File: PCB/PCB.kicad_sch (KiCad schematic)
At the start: 10 parts, among them SW1 Bourns PEC11R, SW2 Bourns PEC11R, SW3 SW_DPST, SW4 SW_DPST, SW5 SW_DPST, U1 RPi_Pico_TH, U2 RDA5807M_Module, U3 LM386

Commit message: finished rev 0 of circuit schematic
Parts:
- added C1: 0.047u, symbol Device:C
- added C2, C3: 470uF, symbol Device:C
- added C4, C5, C6, C7: 0.01uF, Capacitor_THT:C_Disc_D6.0mm_W2.5mm_P5.00mm, symbol Device:C
- added R1, R2: 2k, Resistor_THT:R_Axial_DIN0207_L6.3mm_D2.5mm_P7.62mm_Horizontal, symbol Device:R
- added R10, R11, R4, R5, R6, R7, R8, R9: 10k, Resistor_THT:R_Axial_DIN0207_L6.3mm_D2.5mm_P7.62mm_Horizontal, symbol Device:R
- added R3: 10, Resistor_THT:R_Axial_DIN0207_L6.3mm_D2.5mm_P7.62mm_Horizontal, symbol Device:R
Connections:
- net 3V3: now also SW3.1, SW4.1, SW5.1, C3.2, R1.1, R11.1, R2.1, R4.1, R6.1, R8.1
- net GND: now also DISP1.1 (VSS/GND), LS1.2, U2.6 (GND), U3.2 (-), U3.4 (GND), C3.1, C4.2, C5.2, C6.2, C7.2, R3.2
- net Radio sdio: now reaches U2.1 (SDIO)
- net Radio sdio: now also U1.32 (GP27/ADC1), R1.2
- net antenna: now reaches U2.10 (FMIN)
- net Radio sclk: now reaches U2.2 (SCLK)
- net Radio sclk: now also U1.31 (GP26/ADC0), R2.2
- net at U2.8 (LOUT): now also U3.3 (+)
- net Display sck: now reaches DISP1.3 (SCLK)
- net Display sck: now also U1.24 (GP18)
- net Display sda: now reaches DISP1.4 (SDA)
- net Display sda: now also U1.25 (GP19)
- net Display res: now reaches DISP1.5 (RES)
- net Display res: now also U1.27 (GP21)
- net Display DC: now reaches DISP1.6 (DC)
- net Display DC: now also U1.26 (GP20)
- net Display CS: now reaches DISP1.7 (CS)
- net Display CS: now also U1.22 (GP17)
- net at SW1.A: now also R4.2, R5.1
- net at SW1.B: now also R6.2, R7.1
- net Encoder1SW: now reaches SW1.S2
- net Encoder1SW: now also U1.4 (GP2)
- net B2: now reaches SW4.4
- net B2: now also U1.10 (GP7)
- net Encoder1A: now reaches U1.1 (GP0)
- net Encoder1A: now also C4.1, R5.2
- net B3: now reaches U1.11 (GP8)
- net B3: now also SW5.4
- net Encoder1B: now reaches U1.2 (GP1)
- net Encoder1B: now also C5.1, R7.2
- net Encoder2A: now reaches U1.5 (GP3)
- net Encoder2A: now also C6.1, R9.2
- net Encoder2B: now reaches U1.6 (GP4)
- net Encoder2B: now also C7.1, R10.2
- net Encoder2SW: now reaches U1.7 (GP5)
- net Encoder2SW: now also SW2.S2
- net B1: now reaches U1.9 (GP6)
- net B1: now also SW3.4
- net at SW2.A: now also R8.2, R9.1
- net at SW2.B: now also R10.1, R11.2
- net at LS1.1: now also C2.2
- net at U3.5: now also C1.1, C2.1
- new net: C1.2, R3.1
- no-connect marks 11 -> 30
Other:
- note added: "0"
- note added: "2025/06/20"
- note added: "Watering hole clock radio"
- note added: "Wil Fehr"
- moved on the sheet: DISP1, LS1, SW1, U2, U3

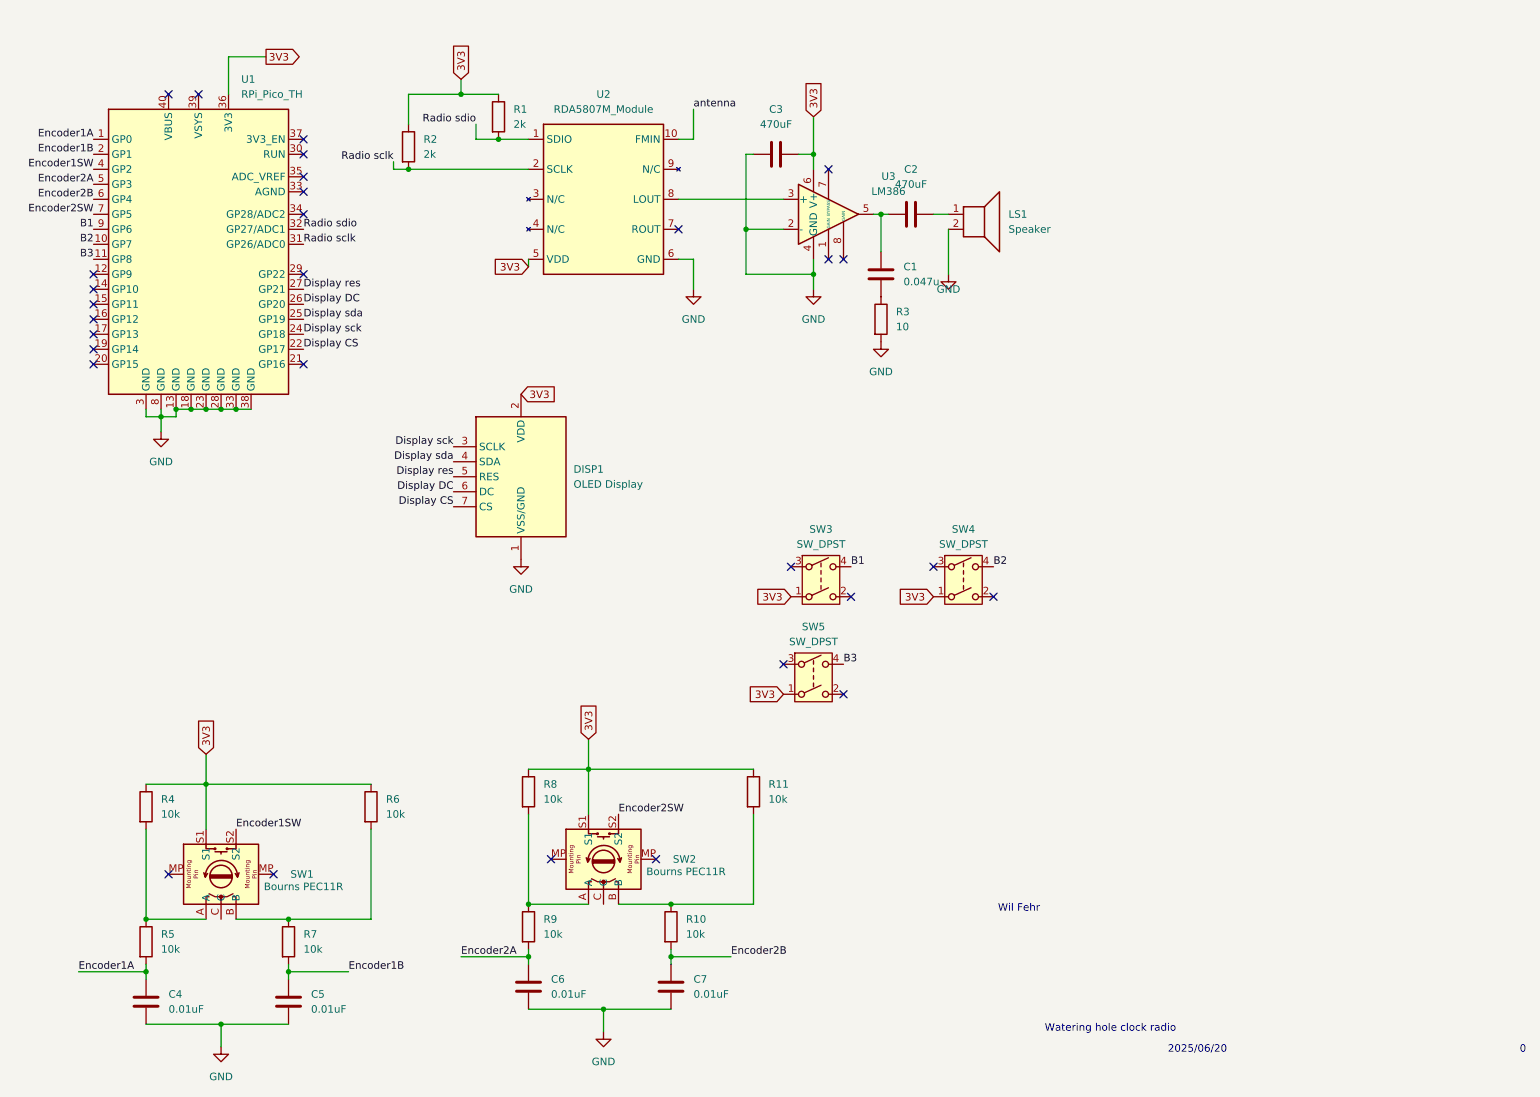
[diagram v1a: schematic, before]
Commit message: Initial look-over
Added footprint for LM386. We will need to decide footprints for resistors, capacitors, etc.

Any two legged through hole components can probably use the same footprint, but some components might be surface mount.
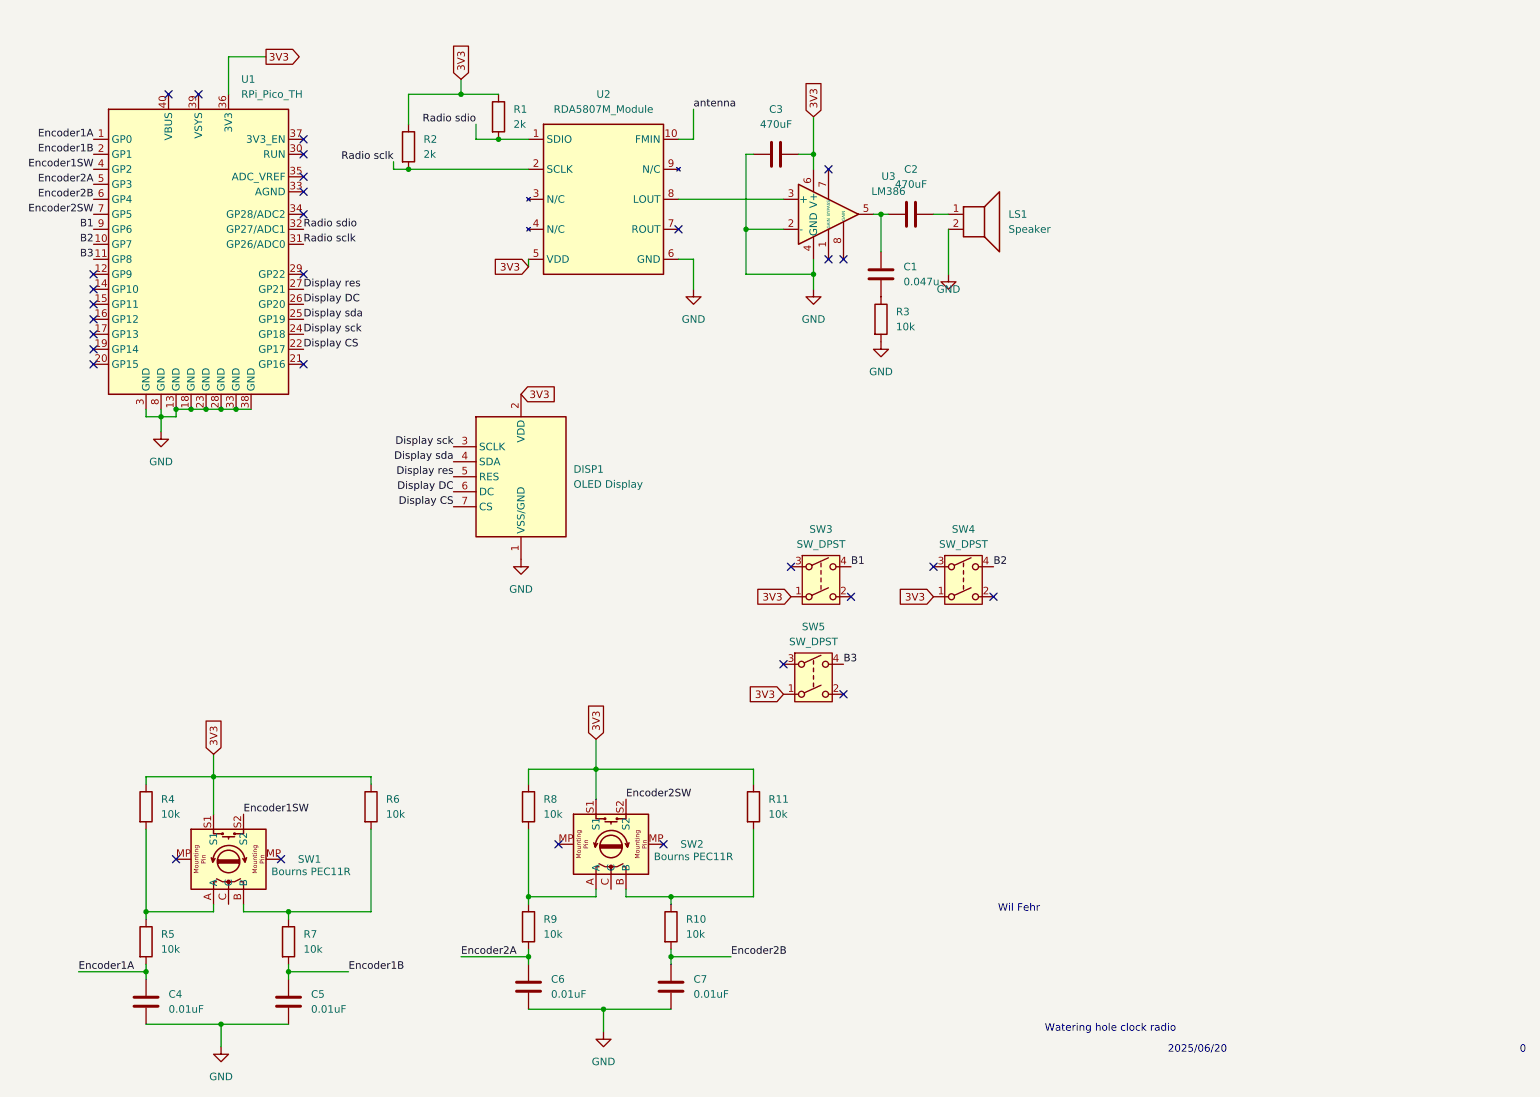
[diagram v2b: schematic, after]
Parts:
- R3: value 10 -> 10k
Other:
- moved on the sheet: R11, R8, SW1, SW2

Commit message: Added footprint to OLED
added 7pin screw terminal footprint to oled. Could not find OLED footprint so with this design we will just wire from OLED to screw terminal block.
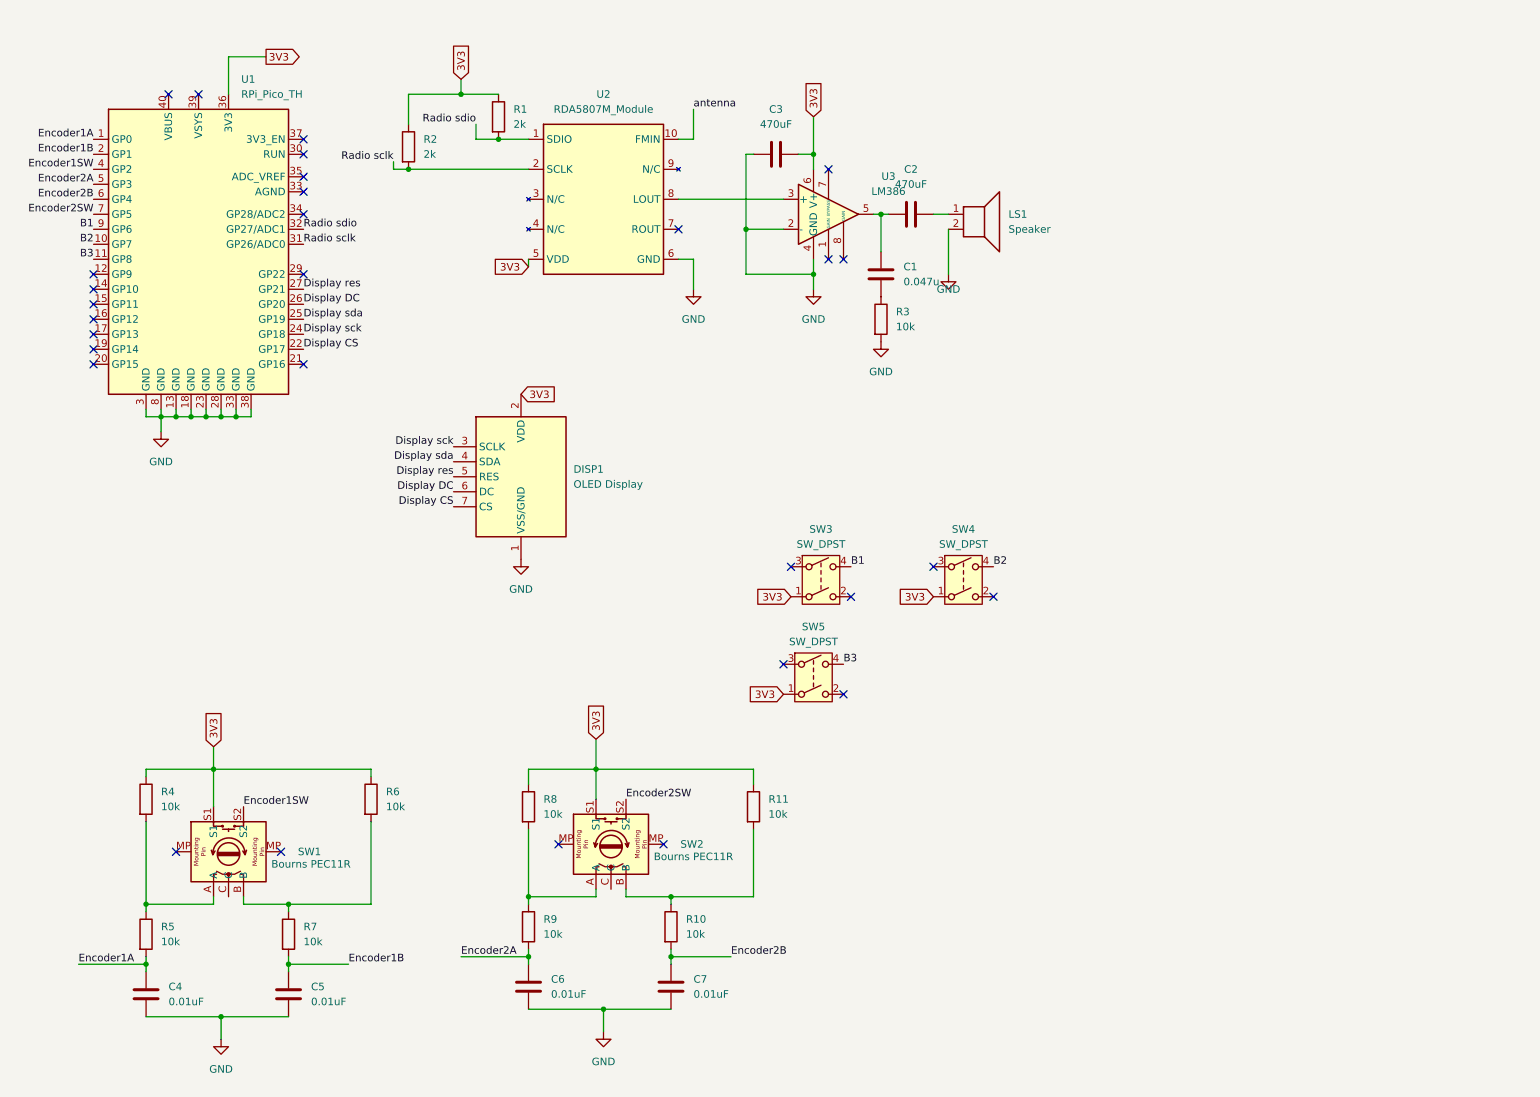
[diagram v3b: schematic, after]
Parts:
- C1, U3: footprint (none) -> LM386N_4_NOPB:DIP794W45P254L959H508Q8
- DISP1: footprint (none) -> 7pin_ScrewTerminal:1727065
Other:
- note removed: "0"
- note removed: "2025/06/20"
- note removed: "Watering hole clock radio"
- note removed: "Wil Fehr"
- company: (none) -> Wil Fehr & Aodhan Tonnesen
- title: (none) -> Watering Hole Clock Radio
- moved on the sheet: C4, C5, R4, R5, R6, R7, SW1

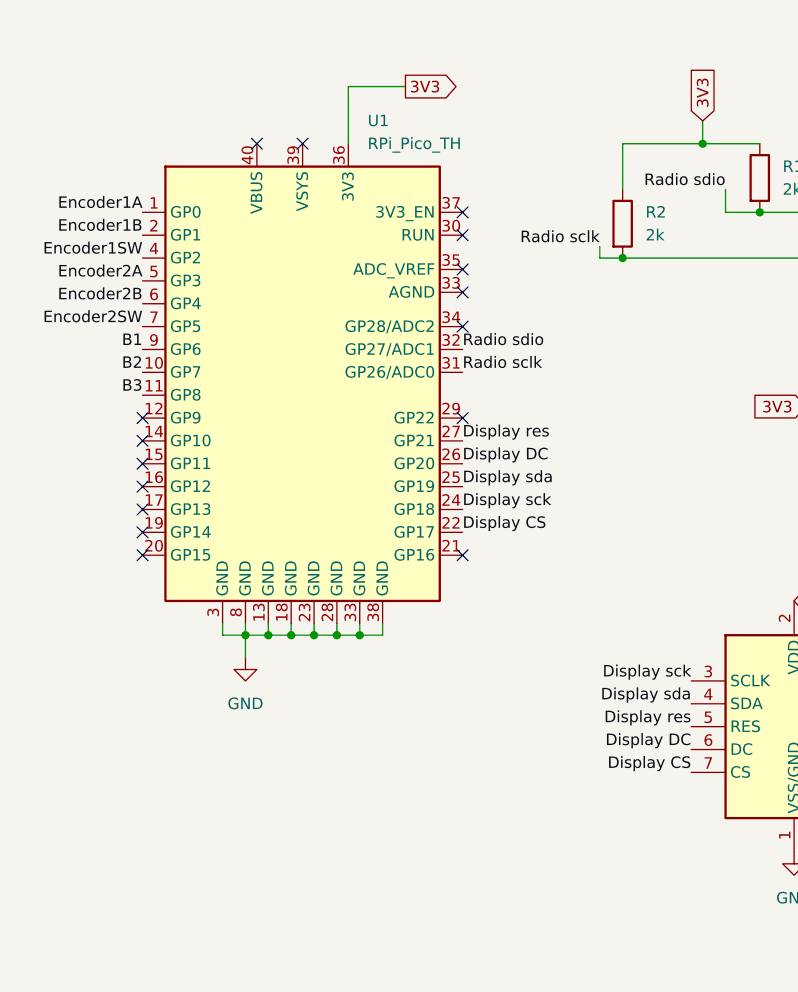
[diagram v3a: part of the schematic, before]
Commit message: Added voltage regulator and battery
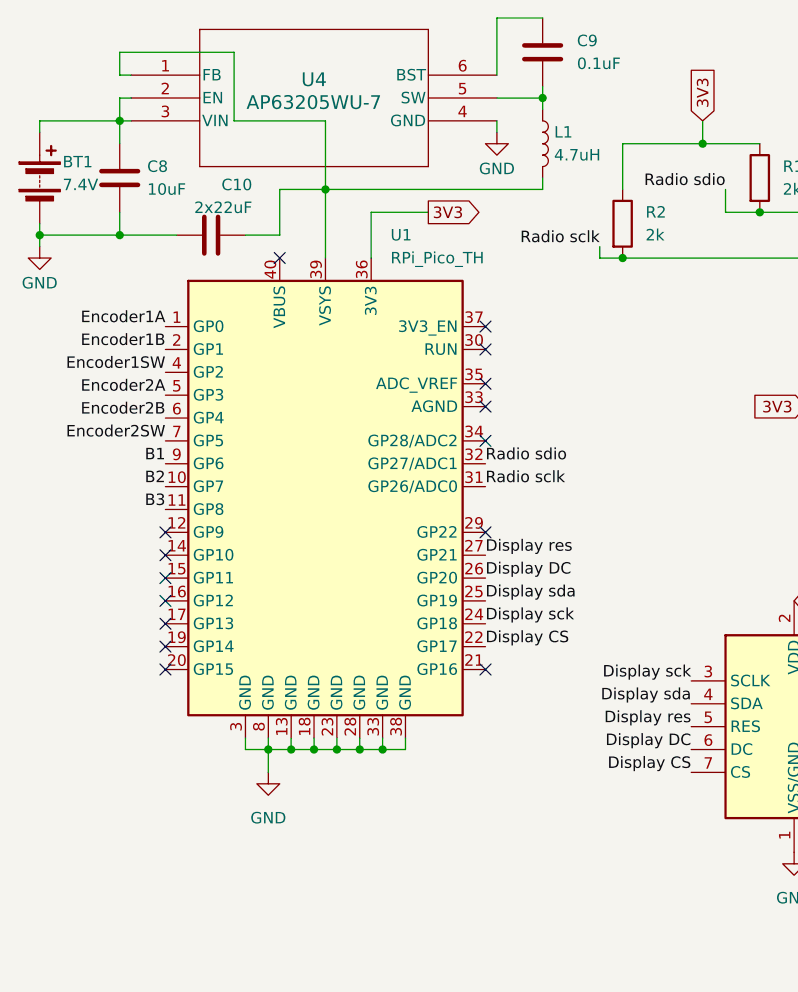
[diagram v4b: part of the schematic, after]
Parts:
- added BT1: 7.4V, symbol Device:Battery
- added C10: 2x22uF, Capacitor_THT:C_Disc_D6.0mm_W2.5mm_P5.00mm, symbol Device:C
- added C8: 10uF, Capacitor_THT:C_Disc_D6.0mm_W2.5mm_P5.00mm, symbol Device:C
- added C9: 0.1uF, Capacitor_THT:C_Disc_D6.0mm_W2.5mm_P5.00mm, symbol Device:C
- added L1: 4.7uH, symbol Device:L
- added U4: AP63205WU-7, footprints:SOIC_05WU-7_DIO, symbol 2025-06-24_23-02-35:AP63205WU-7
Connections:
- net GND: now also BT1.2 (-), C10.1, C8.2, U4.4 (GND)
- net at U1.39 (VSYS): now also C10.2, L1.2, U4.1 (FB)
- new net: C9.2, L1.1, U4.5 (SW)
- new net: BT1.1 (+), C8.1, U4.2 (EN), U4.3 (VIN)
- new net: C9.1, U4.6 (BST)
- no-connect marks 30 -> 29
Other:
- moved on the sheet: U1

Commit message: More fiddling
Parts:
- C1: footprint LM386N_4_NOPB:DIP794W45P254L959H508Q8 -> Capacitor_THT:C_Disc_D6.0mm_W2.5mm_P5.00mm
- C2, C3: footprint (none) -> Capacitor_THT:C_Disc_D6.0mm_W2.5mm_P5.00mm
- L1: footprint (none) -> Inductor_SMD:L_0805_2012Metric_Pad1.15x1.40mm_HandSolder
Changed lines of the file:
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@@
 			)
 		)
-		(property "Footprint" ""
+		(property "Footprint" "Capacitor_THT:C_Disc_D6.0mm_W2.5mm_P5.00mm"
 			(at 168.91 51.1048 0)
 			(effects
@@
 			)
 		)
-		(property "Footprint" ""
+		(property "Footprint" "Inductor_SMD:L_0805_2012Metric_Pad1.15x1.40mm_HandSolder"
 			(at 71.12 31.75 0)
 			(effects
@@
 			)
 		)
-		(property "Footprint" "LM386N_4_NOPB:DIP794W45P254L959H508Q8"
+		(property "Footprint" "Capacitor_THT:C_Disc_D6.0mm_W2.5mm_P5.00mm"
 			(at 160.9852 66.04 0)
 			(effects
@@
 			)
 		)
-		(property "Footprint" ""
+		(property "Footprint" "Capacitor_THT:C_Disc_D6.0mm_W2.5mm_P5.00mm"
 			(at 146.05 40.9448 0)
 			(effects

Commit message: PCB design #1
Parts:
- added C11: 2x22uF, Capacitor_SMD:C_1206_3216Metric, symbol Device:C
- BT1: footprint (none) -> Battery:THT Battery Connection
- C10, C8: footprint Capacitor_THT:C_Disc_D6.0mm_W2.5mm_P5.00mm -> Capacitor_SMD:C_1206_3216Metric
- C9: footprint Capacitor_THT:C_Disc_D6.0mm_W2.5mm_P5.00mm -> Capacitor_SMD:C_0805_2012Metric
- L1: footprint Inductor_SMD:L_0805_2012Metric_Pad1.15x1.40mm_HandSolder -> Inductor_SMD:L_Cenker_CKCS201610
- LS1, SW3, SW4, SW5: footprint (none) -> 2pin_ScrewTerminal:691137710002
- SW1, SW2: footprint Rotary_Encoder:RotaryEncoder_Alps_EC12E-Switch_Vertical_H20mm -> 5pin_ScrewTerminal:PHOENIX_1935190
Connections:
- net B1: now also SW3.2; no longer SW3.4
- net B2: now also SW4.2; no longer SW4.4
- net B3: now also SW5.2; no longer SW5.4
- net GND: now also C11.1
- net at C10.2, L1.2, U1.39 (VSYS)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: now also C11.2
- no-connect marks 29 -> 25

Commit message: updated schematic
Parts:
- added C12: 470uF, Capacitor_THT:C_Disc_D6.0mm_W2.5mm_P5.00mm, symbol Device:C
- added R12: 1k, Resistor_THT:R_Axial_DIN0207_L6.3mm_D2.5mm_P7.62mm_Horizontal, symbol Device:R
- added R13: 150, Resistor_THT:R_Axial_DIN0207_L6.3mm_D2.5mm_P7.62mm_Horizontal, symbol Device:R
- C3: value 470uF -> 10uF
- R3: value 10k -> 10
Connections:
- net 3V3: no longer C3.2, U3.6 (V+)
- net GND: now also SW1.C, SW2.C, R13.2; no longer C3.1, U3.2 (-)
- net 5V: now reaches C10.2, C11.2, L1.2, U1.39 (VSYS), U4.1 (FB)
- net 5V: now also C3.2, U3.6 (V+)
- net at U2.8 (LOUT): now also R12.1; no longer U3.3 (+)
- new net: C12.1, R12.2, R13.1
- new net: C12.2, U3.3 (+)
- new net: C3.1, U3.2 (-)
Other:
- moved on the sheet: C1, C2, C3, LS1, R3, U3

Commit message: updated footprints
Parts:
- C12, C2: footprint Capacitor_THT:C_Disc_D6.0mm_W2.5mm_P5.00mm -> Capacitor_THT:C_Radial_D6.3mm_H11.0mm_P2.50mm
- C3: footprint Capacitor_THT:C_Disc_D6.0mm_W2.5mm_P5.00mm -> Capacitor_THT:C_Radial_D5.0mm_H11.0mm_P2.00mm
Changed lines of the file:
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@@
 		(title "Watering Hole Clock Radio")
 		(date "2025-06-24")
-		(rev "1")
+		(rev "2")
 		(company "Wil Fehr & Aodhan Tonnesen")
 	)
@@
 			)
 		)
-		(property "Footprint" "Capacitor_THT:C_Disc_D6.0mm_W2.5mm_P5.00mm"
+		(property "Footprint" "Capacitor_THT:C_Radial_D6.3mm_H11.0mm_P2.50mm"
 			(at 190.5 51.1048 0)
 			(effects
@@
 			)
 		)
-		(property "Footprint" "Capacitor_THT:C_Disc_D6.0mm_W2.5mm_P5.00mm"
+		(property "Footprint" "Capacitor_THT:C_Radial_D6.3mm_H11.0mm_P2.50mm"
 			(at 156.21 56.1848 0)
 			(effects
@@
 			)
 		)
-		(property "Footprint" "Capacitor_THT:C_Disc_D6.0mm_W2.5mm_P5.00mm"
+		(property "Footprint" "Capacitor_THT:C_Radial_D5.0mm_H11.0mm_P2.00mm"
 			(at 167.64 40.9448 0)
 			(effects
